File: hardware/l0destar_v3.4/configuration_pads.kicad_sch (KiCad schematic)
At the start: 5 parts

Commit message: change references to ISO-9141 to k-wire
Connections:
- net CAN_H_ISO9141_K renamed CAN_H_KWIRE_K
- net CAN_L_ISO9141_L renamed CAN_L_KWIRE_L
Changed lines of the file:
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@@
 		)
 	)
-	(global_label "CAN_L_ISO9141_L"
+	(global_label "CAN_L_KWIRE_L"
 		(shape input)
 		(at 40.64 60.96 180)
@@
 		)
 		(property "Intersheetrefs" "${INTERSHEET_REFS}"
-			(at 21.0239 60.96 0)
+			(at 23.2615 60.96 0)
 			(hide yes)
 			(show_name no)
@@
 		)
 	)
-	(global_label "CAN_H_ISO9141_K"
+	(global_label "CAN_H_KWIRE_K"
 		(shape input)
 		(at 40.64 35.56 180)
@@
 		)
 		(property "Intersheetrefs" "${INTERSHEET_REFS}"
-			(at 20.4796 35.56 0)
+			(at 22.7172 35.56 0)
 			(hide yes)
 			(show_name no)

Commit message: doc updates
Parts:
- S5R1, S5R2, S5R3, S5R4, S5R5: now not fitted
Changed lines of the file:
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@@
 		(on_board yes)
 		(in_pos_files yes)
-		(dnp no)
+		(dnp yes)
 		(fields_autoplaced yes)
 		(property "Reference" "S5R3"
@@
 		(on_board yes)
 		(in_pos_files yes)
-		(dnp no)
+		(dnp yes)
 		(fields_autoplaced yes)
 		(property "Reference" "S5R1"
@@
 		(on_board yes)
 		(in_pos_files yes)
-		(dnp no)
+		(dnp yes)
 		(fields_autoplaced yes)
 		(property "Reference" "S5R4"
@@
 		(on_board yes)
 		(in_pos_files yes)
-		(dnp no)
+		(dnp yes)
 		(fields_autoplaced yes)
 		(property "Reference" "S5R5"
@@
 		(on_board yes)
 		(in_pos_files yes)
-		(dnp no)
+		(dnp yes)
 		(fields_autoplaced yes)
 		(property "Reference" "S5R2"

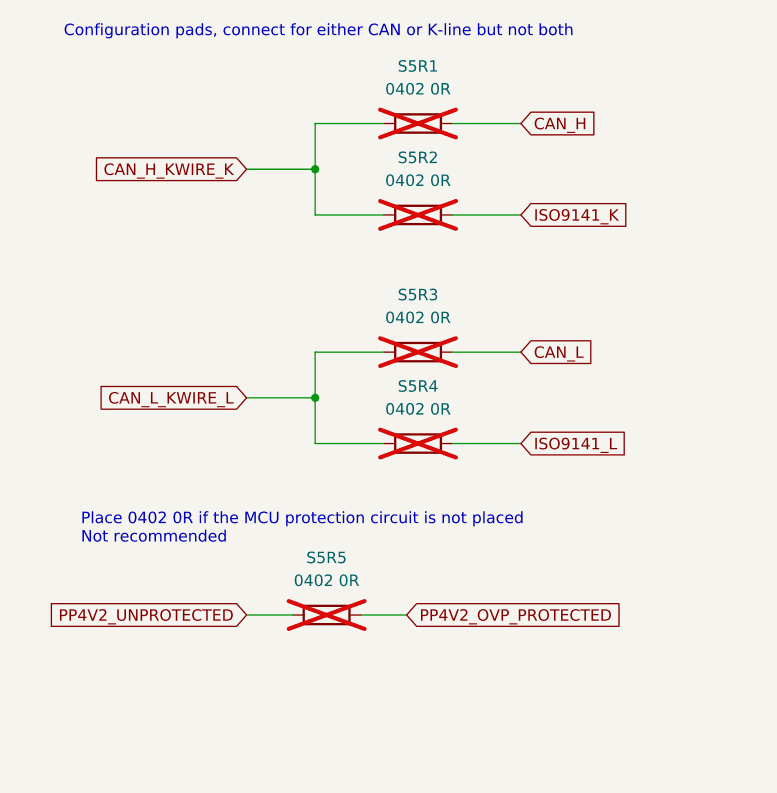
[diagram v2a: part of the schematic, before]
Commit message: swap INA228 for INA238
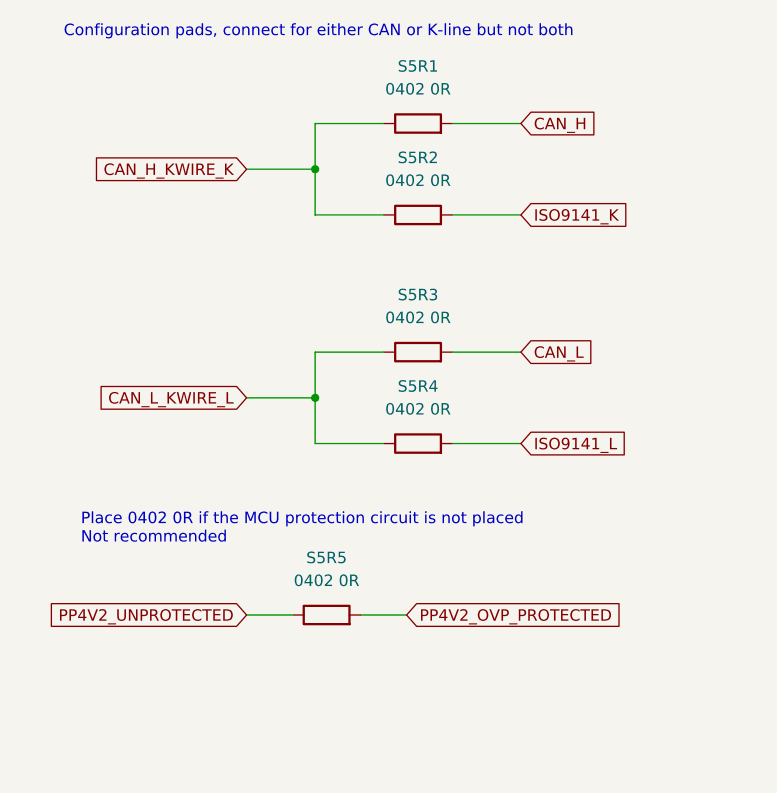
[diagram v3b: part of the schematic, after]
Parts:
- S5R1, S5R2, S5R3, S5R4, S5R5: now fitted
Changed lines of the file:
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@@
 		(on_board yes)
 		(in_pos_files yes)
-		(dnp yes)
+		(dnp no)
 		(fields_autoplaced yes)
 		(property "Reference" "S5R3"
@@
 		(on_board yes)
 		(in_pos_files yes)
-		(dnp yes)
+		(dnp no)
 		(fields_autoplaced yes)
 		(property "Reference" "S5R1"
@@
 		(on_board yes)
 		(in_pos_files yes)
-		(dnp yes)
+		(dnp no)
 		(fields_autoplaced yes)
 		(property "Reference" "S5R4"
@@
 		(on_board yes)
 		(in_pos_files yes)
-		(dnp yes)
+		(dnp no)
 		(fields_autoplaced yes)
 		(property "Reference" "S5R5"
@@
 		(on_board yes)
 		(in_pos_files yes)
-		(dnp yes)
+		(dnp no)
 		(fields_autoplaced yes)
 		(property "Reference" "S5R2"
